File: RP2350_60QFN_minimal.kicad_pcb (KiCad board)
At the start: 2 copper layers, 105.5 x 65.5 mm, 73 parts, among them J1 USB_B_Micro, J2 Conn_02x18_Odd_Even, J3 Conn_02x18_Odd_Even, J4 SM03B-SRSS-TB, SW1 SW_Push, SW2 SW_Push, U1 RP2350_60QFN, U2 NCP1117-3.3_SOT223, U3 W25Q128JVS, U4 CD74HC4067SM96G4, U5 TLV9002IDGKR, U6 ADS1115IDGSR, U7 PCA9306, Y2 ABM8-272-T3

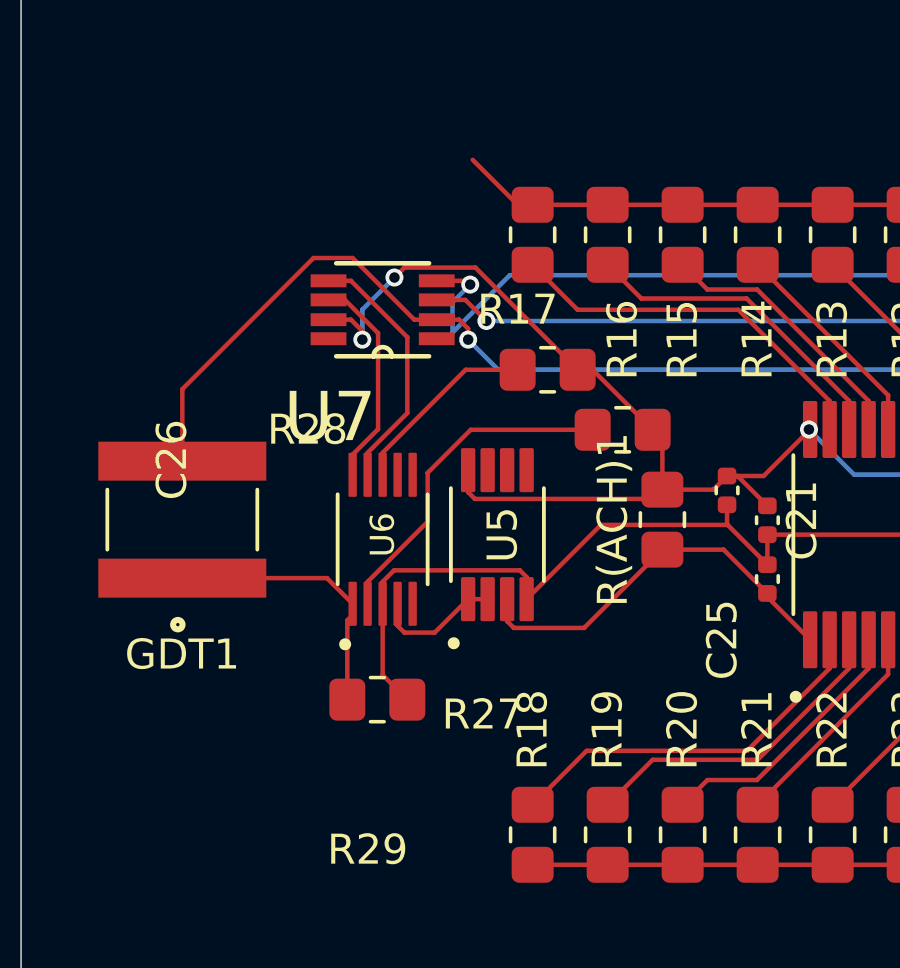
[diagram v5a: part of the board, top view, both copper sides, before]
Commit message: update shematic names
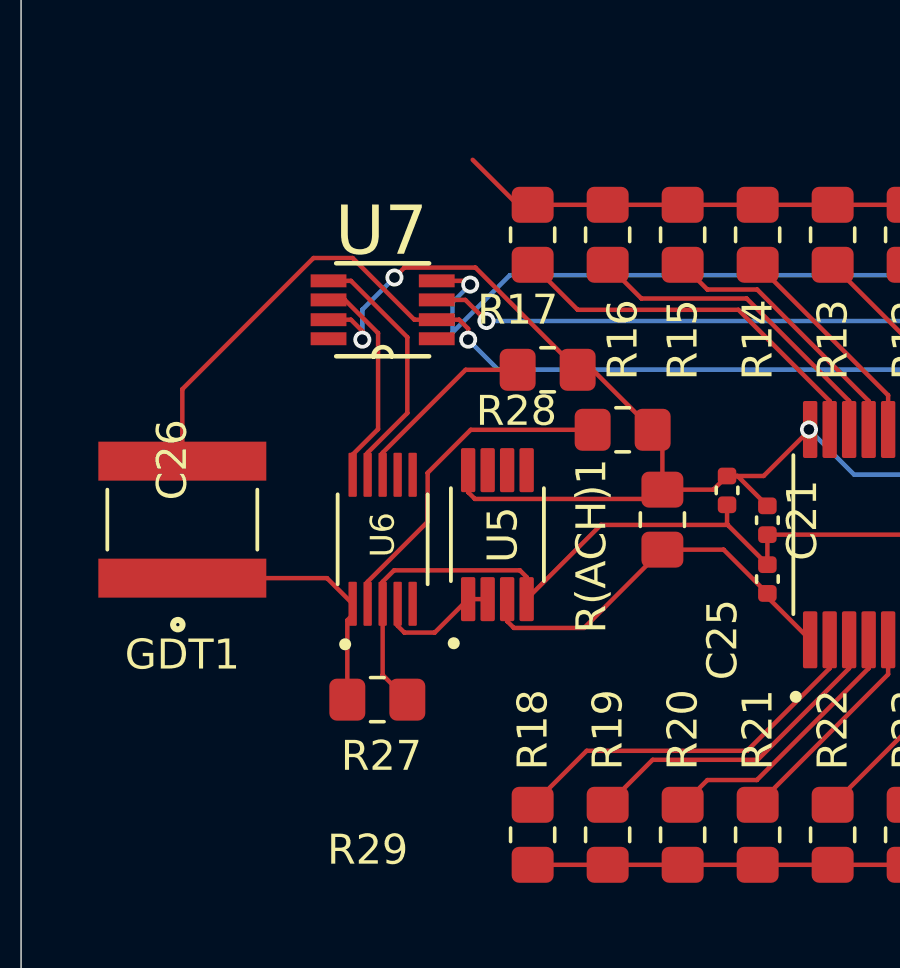
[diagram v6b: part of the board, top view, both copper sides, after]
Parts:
- U5: value TLV9002IDGKR -> TLV900
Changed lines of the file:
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@@
 		(tags "resistor handsolder")
 		(property "Reference" "R27"
-			(at -3.5 -0.5 360)
+			(at -0.13625 -1.876999 0)
 			(layer "F.SilkS")
 			(effects
@@
 		)
 		(property "Value" "10k"
-			(at 3.5 0 360)
+			(at 3.5 0 0)
 			(layer "F.Fab")
 			(effects
@@
 		)
 		(fp_text user "${REFERENCE}"
-			(at 0 0 360)
+			(at 0 0 0)
 			(layer "F.Fab")
 			(effects
@@
 		(tags "resistor handsolder")
 		(property "Reference" "R(ACH)1"
-			(at 0 -1.65 90)
+			(at -0.876999 -2.36625 -90)
 			(layer "F.SilkS")
 			(effects
@@
 		(tags "resistor handsolder")
 		(property "Reference" "R17"
-			(at -2.5 -0.5 360)
+			(at -2.5 -0.5 0)
 			(layer "F.SilkS")
 			(effects
@@
 			)
 		)
-		(property "Value" "TLV9002IDGKR"
-			(at -4.505 -0.825 90)
+		(property "Value" "TLV900"
+			(at -4.376999 1.63375 180)
 			(layer "F.Fab")
 			(effects
@@
 		(at 126.54125 68.128001 180)
 		(property "Reference" "U7"
-			(at 1.753665 -3.583585 360)
+			(at 0.04125 2.628001 0)
 			(layer "F.SilkS")
 			(effects
@@
 		)
 		(property "Footprint" "PCA9306DP1_125:SOP65P400X110-8N"
-			(at 0 0 360)
+			(at 0 0 0)
 			(layer "F.Fab")
 			(hide yes)
@@
 		)
 		(property "Datasheet" ""
-			(at 0 0 360)
+			(at 0 0 0)
 			(layer "F.Fab")
 			(hide yes)
@@
 		)
 		(property "Description" ""
-			(at 0 0 360)
+			(at 0 0 0)
 			(layer "F.Fab")
 			(hide yes)
@@
 		(tags "resistor handsolder")
 		(property "Reference" "R29"
-			(at -8.5 14 360)
+			(at -8.5 14 0)
 			(layer "F.SilkS")
 			(effects
@@
 		)
 		(property "Value" "10k"
-			(at -6.5 17.5 360)
+			(at -6.5 17.5 0)
 			(layer "F.Fab")
 			(effects
@@
 		)
 		(fp_text user "${REFERENCE}"
-			(at 0 0 360)
+			(at 0 0 0)
 			(layer "F.Fab")
 			(effects
@@
 		(tags "resistor handsolder")
 		(property "Reference" "R28"
-			(at -8 2 360)
+			(at -1.04125 1.371999 0)
 			(layer "F.SilkS")
 			(effects
@@
 		)
 		(property "Value" "10k"
-			(at -5.5 5.5 360)
+			(at -3.54125 0.871999 90)
 			(layer "F.Fab")
 			(effects
@@
 		)
 		(fp_text user "${REFERENCE}"
-			(at 0 0 360)
+			(at 0 0 0)
 			(layer "F.Fab")
 			(effects
@@
 		(at 119.86375 75.123001 90)
 		(property "Reference" "GDT1"
-			(at -4.5 0 360)
+			(at -4.5 0 0)
 			(layer "F.SilkS")
 			(effects
